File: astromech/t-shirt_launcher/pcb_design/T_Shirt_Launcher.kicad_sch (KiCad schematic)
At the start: 15 parts, among them J1 Conn_01x02_Socket, J2 Conn_01x02_Socket, U1 ESP32-C6-DEVKITC-1-N8, U2 D36V50F5_Pololu, U3 ADA4510-2ARZ, U4 ADA4510-2ARZ, U5 MAX22203AUU+, U6 ADP3634ARDZ, U7 SN74LVC1G19DBVR, U8 SN74LVC1G19DBVR

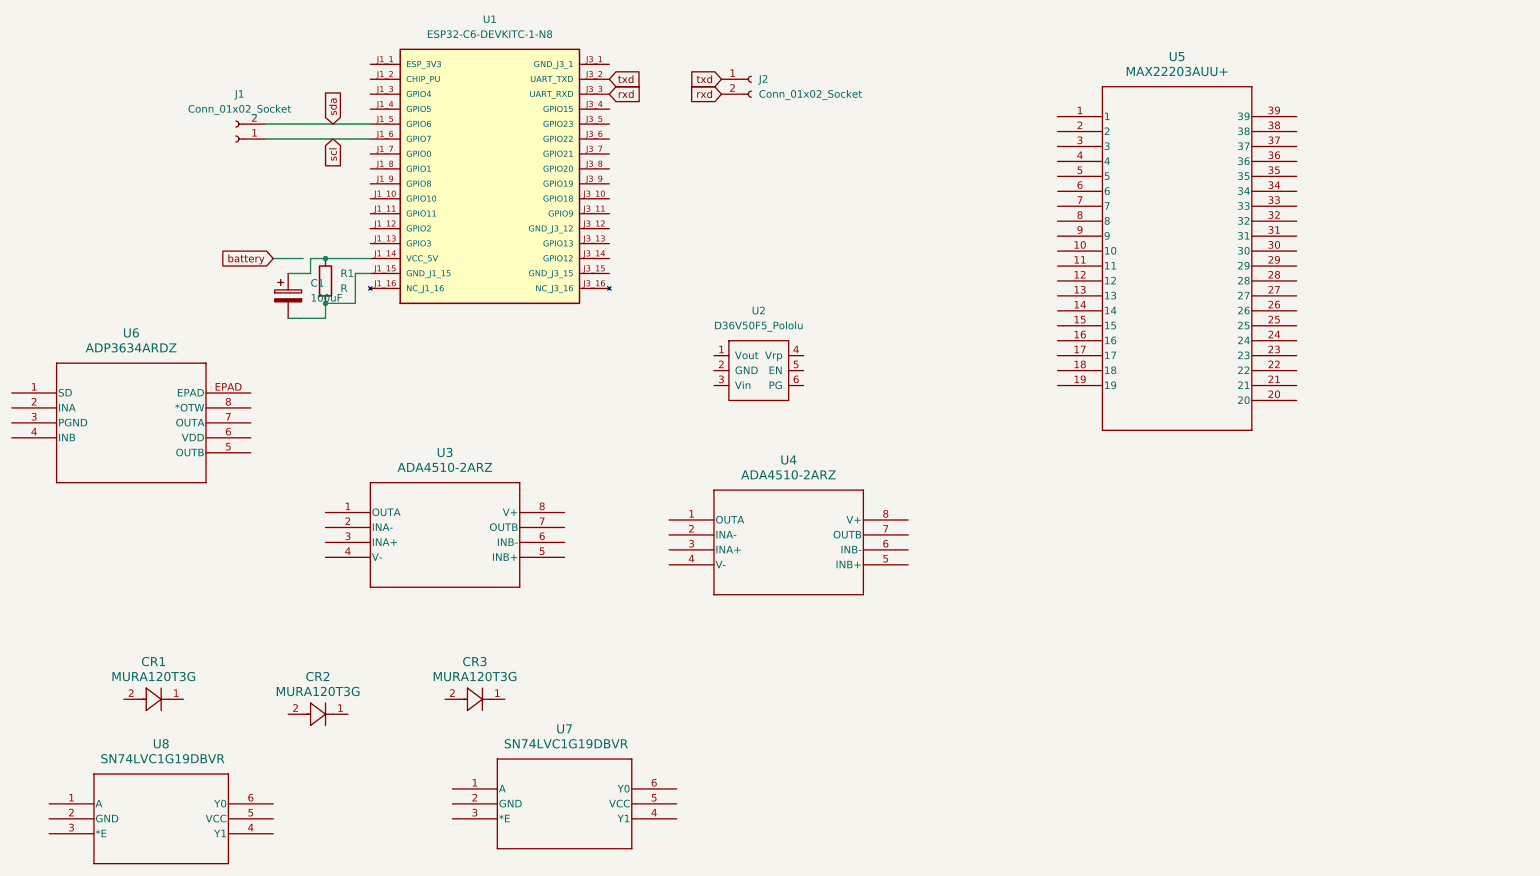
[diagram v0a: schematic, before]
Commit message: added some new parts and updated symbols to fit better on schematic
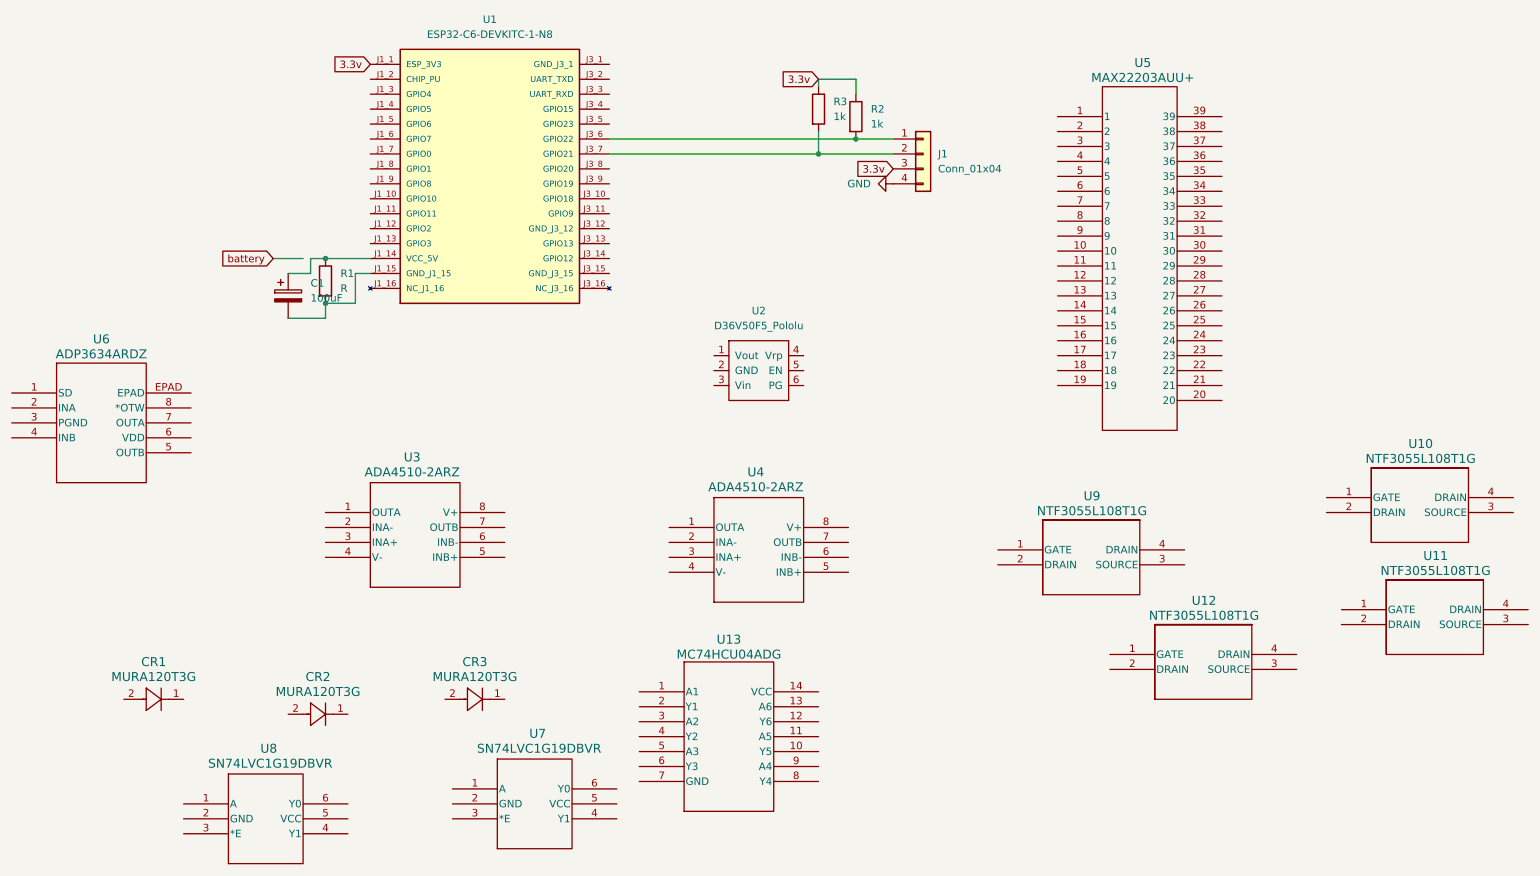
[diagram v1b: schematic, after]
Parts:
- removed J1, J2: Conn_01x02_Socket, Connector_PinSocket_1.27mm:PinSocket_1x02_P1.27mm_Vertical, symbol Connector:Conn_01x02_Socket
- added J1: Conn_01x04, symbol Connector_Generic:Conn_01x04
- added R2, R3: 1k, symbol Device:R
- added U10, U11, U12, U9: NTF3055L108T1G, SOT-223_3P7X6P7_ONS, symbol NTF3055L108T1G:NTF3055L108T1G
- added U13: MC74HCU04ADG, SOIC-14_NB_ONS, symbol MC74HCU04ADG:MC74HCU04ADG
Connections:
- net 3.3v: now reaches U1.J1_1 (ESP_3V3)
- net 3.3v: now also J1.3 (Pin_3), R2.1, R3.1
- net at U1.J3_6 (GPIO22): now also J1.1 (Pin_1), R2.2
- net at U1.J3_7 (GPIO21): now also J1.2 (Pin_2), R3.2
- net rxd: no longer names the net of U1.J3_3 (UART_RXD)
- net scl: no longer names the net of U1.J1_6 (GPIO7)
- net sda: no longer names the net of U1.J1_5 (GPIO6)
- net txd: no longer names the net of U1.J3_2 (UART_TXD)
- new net GND: J1.4 (Pin_4)
